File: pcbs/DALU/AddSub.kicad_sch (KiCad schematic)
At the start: 6 parts, among them U401 74HC86, U402 74HC86, U403 74HC86, U404 74HC283, U405 74HC283, U406 74HC245

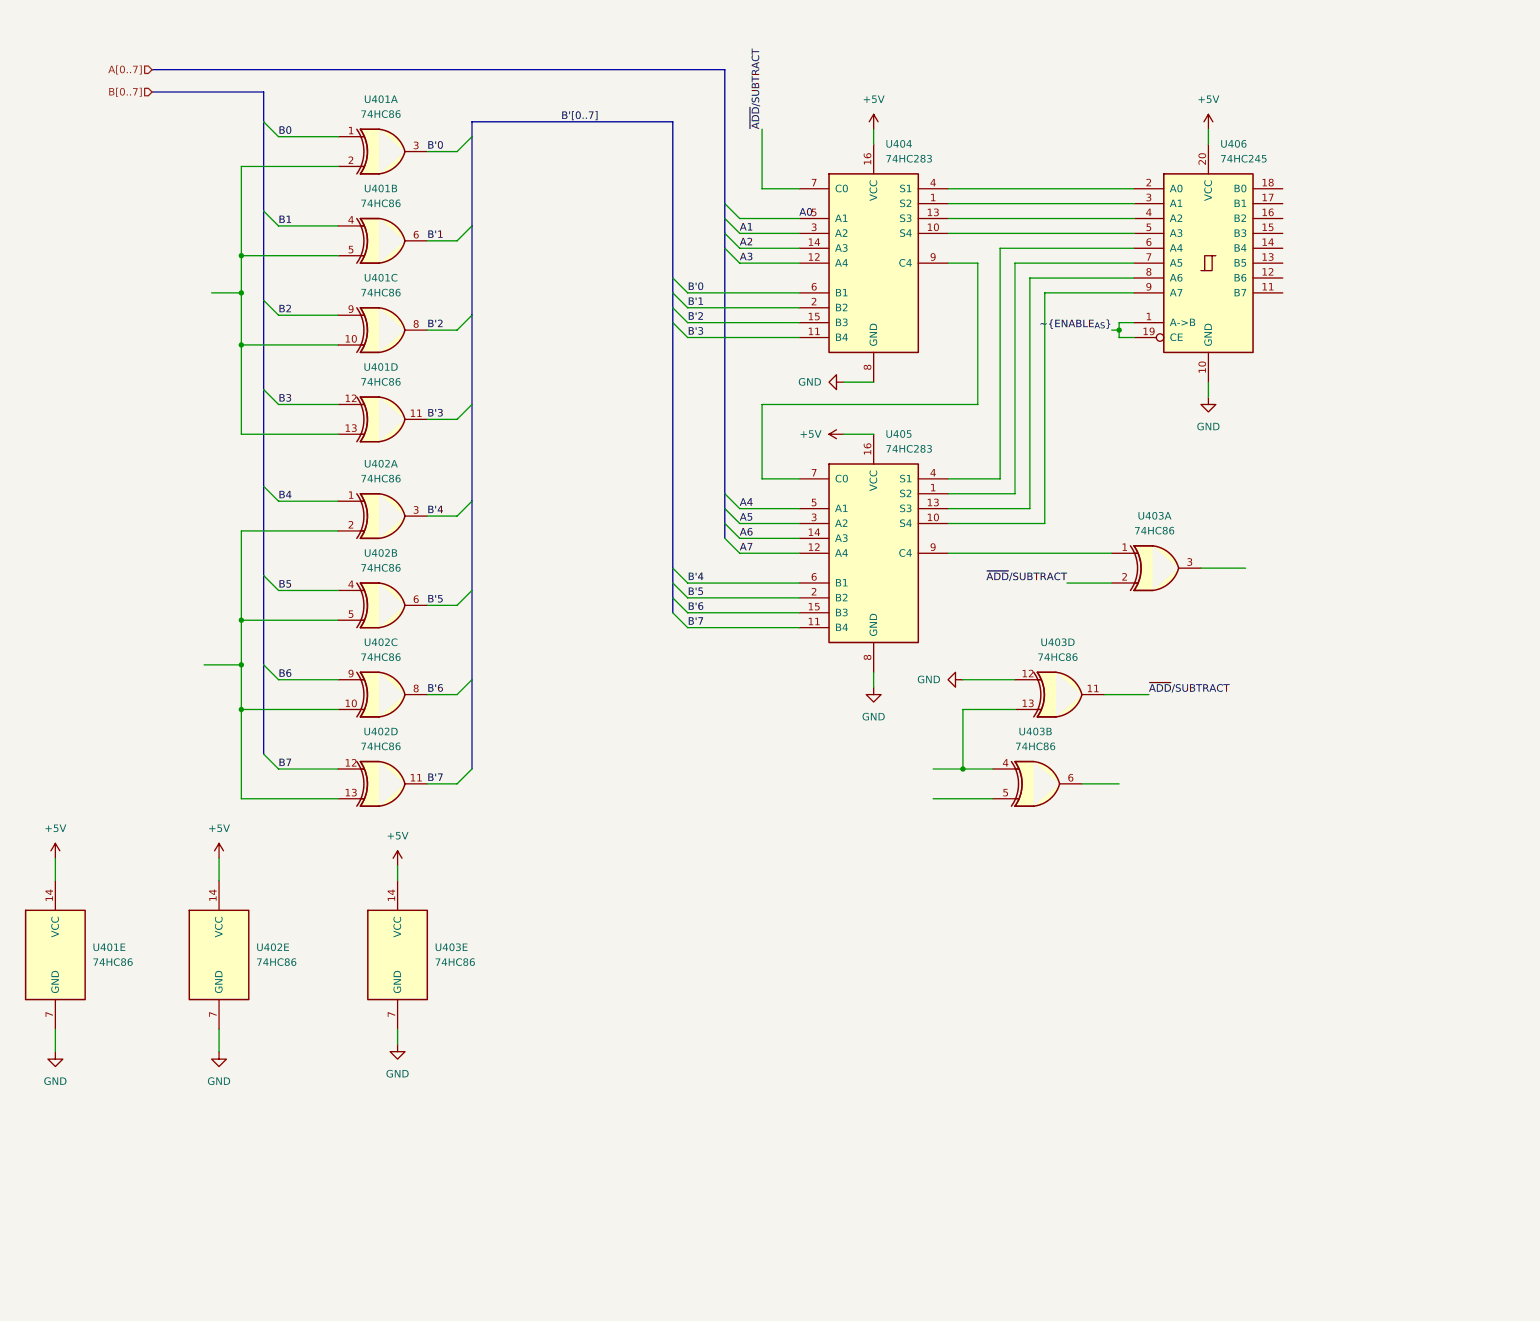
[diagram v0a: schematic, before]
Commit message: Starting to do the routing. Schematic not yet complete, though
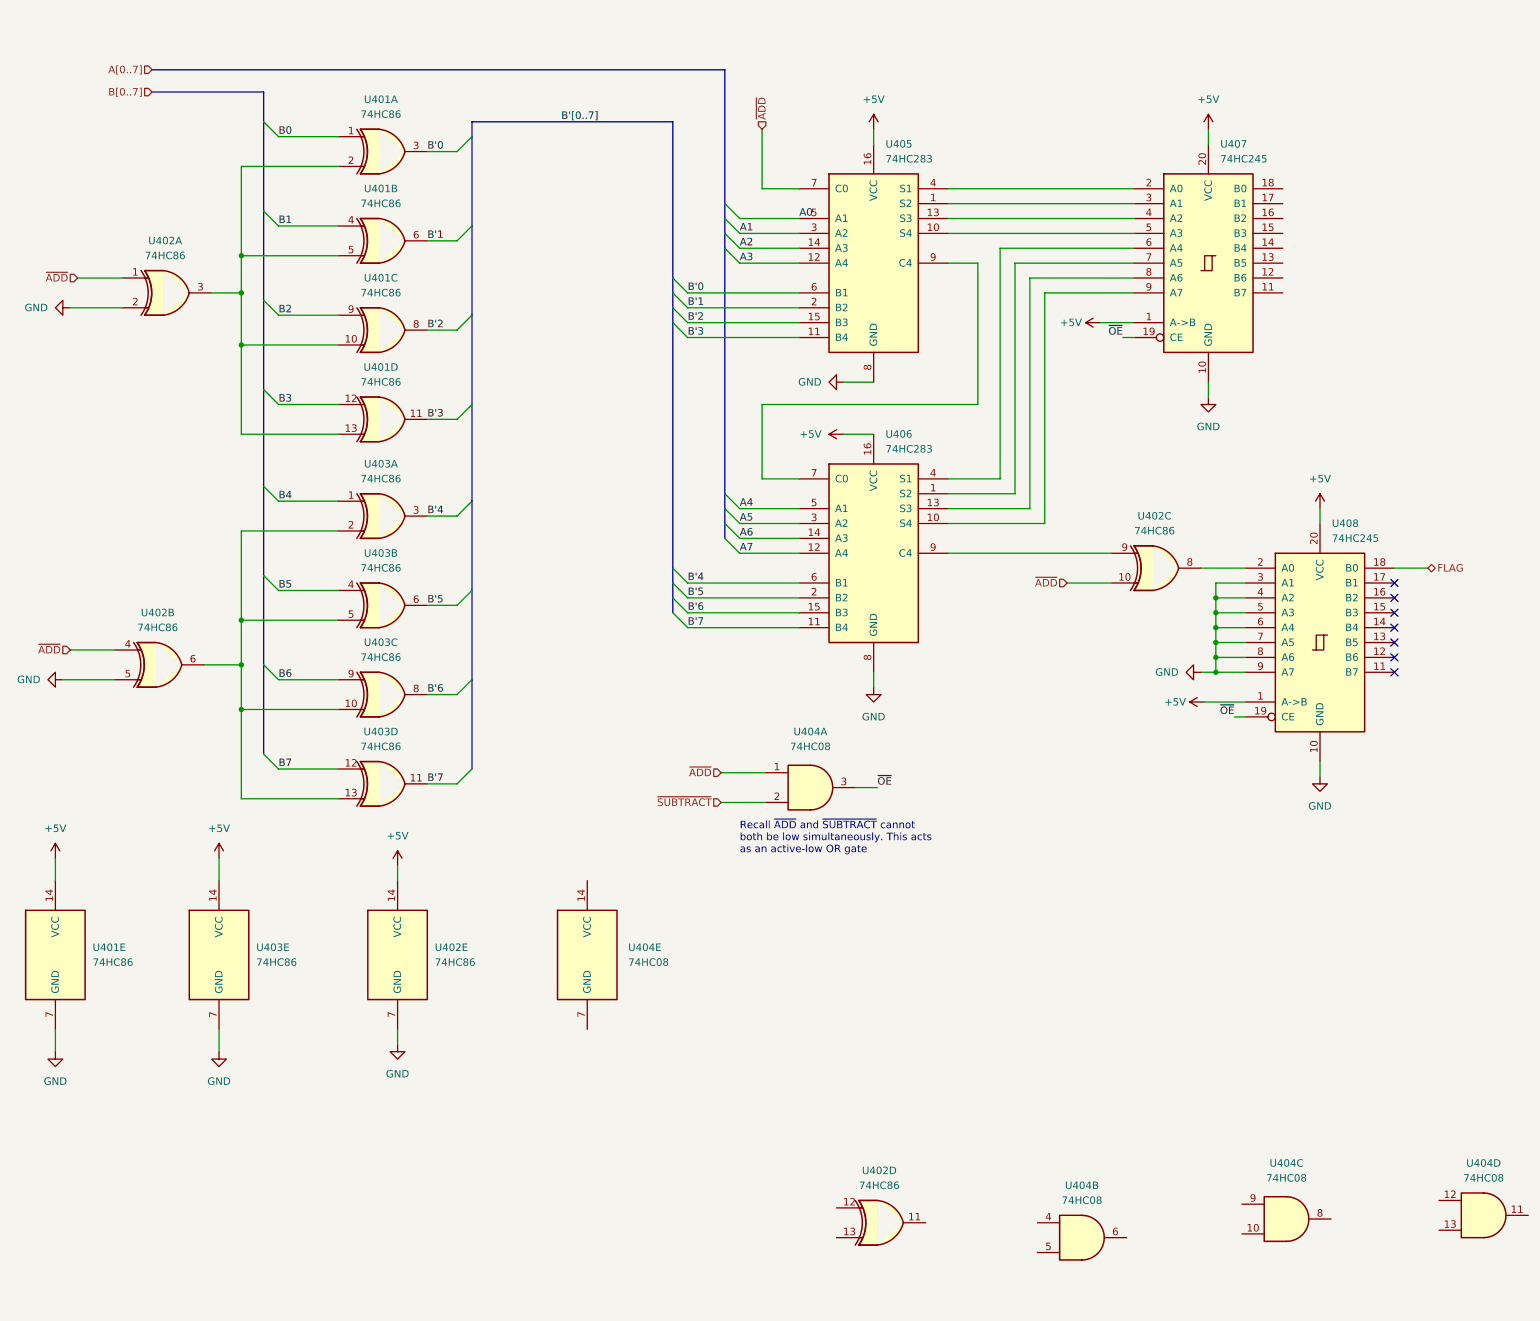
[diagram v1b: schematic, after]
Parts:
- added unit 3 of U402
- added U404: 74HC08, Package_SO:SOIC-14_3.9x8.7mm_P1.27mm, symbol 74xx:74LS08
- added U408: 74HC245, Package_SO:SOIC-20W_7.5x12.8mm_P1.27mm, symbol 74xx:74HC245
- renumbered U403 to U402, U402 to U403, U404 to U405, U405 to U406, U406 to U407
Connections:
- net +5V: now also U407.1 (A->B), U408.1 (A->B), U408.20 (VCC)
- net GND: now also U402.2, U402.5, U408.10 (GND), U408.3 (A1), U408.4 (A2), U408.5 (A3), U408.6 (A4), U408.7 (A5), U408.8 (A6), U408.9 (A7); no longer U402.12
- net at U402.13: no longer U402.4
- net at U401.10, U401.13, U401.2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: now also U402.3
- net at U402.6: now also U403.10, U403.13, U403.2, U403.5
- net at U406.9 (C4): now also U402.9; no longer U402.1
- removed net ~{ADD}/SUBTRACT: U402.11, U402.2, U405.7 (C0)
- net ~{ENABLE_{AS}} renamed ~{OE}
- net ~{OE}: now also U404.3, U408.19 (CE); no longer U407.1 (A->B)
- new net: U402.8, U408.2 (A0)
- new net FLAG: U408.18 (B0)
- new net ~{ADD}: U402.1, U402.10, U402.4, U404.1, U405.7 (C0)
- new net ~{SUBTRACT}: U404.2
- no-connect marks 0 -> 7
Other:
- note added: "Recall ~{ADD} and ~{SUBTRACT} cannot both be low simultaneously. This acts as an active-low OR gate"
- moved on the sheet: U402A, U402B, U402D

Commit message: Fiddling with the adders
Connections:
- net B'0: now also U401.8; no longer U401.3
- net B'1: now also U401.11; no longer U401.6
- net B'2: now also U401.3; no longer U401.8
- net B'3: now also U401.6; no longer U401.11
- net B'4: now also U403.8; no longer U403.3
- net B'5: now also U403.11; no longer U403.6
- net B'6: now also U403.3; no longer U403.8
- net B'7: now also U403.6; no longer U403.11
- net B0: now also U401.9; no longer U401.1
- net B1: now also U401.12; no longer U401.4
- net B2: now also U401.1; no longer U401.9
- net B3: now also U401.4; no longer U401.12
- net B4: now also U403.9; no longer U403.1
- net B5: now also U403.12; no longer U403.4
- net B6: now also U403.1; no longer U403.9
- net B7: now also U403.4; no longer U403.12
- net S_{1}: now reaches U405.1 (S2), U407.3 (A1)
- net S_{3}: now reaches U405.10 (S4), U407.5 (A3)
- net S_{2}: now reaches U405.13 (S3), U407.4 (A2)
- net S_{0}: now reaches U405.4 (S1), U407.2 (A0)
- net S_{5}: now reaches U406.1 (S2), U407.7 (A5)
- net S_{7}: now reaches U406.10 (S4), U407.9 (A7)
- net S_{6}: now reaches U406.13 (S3), U407.8 (A6)
- net S_{4}: now reaches U406.4 (S1), U407.6 (A4)
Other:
- moved on the sheet: U401A, U401B, U401C, U401D, U403A, U403B, U403C, U403D

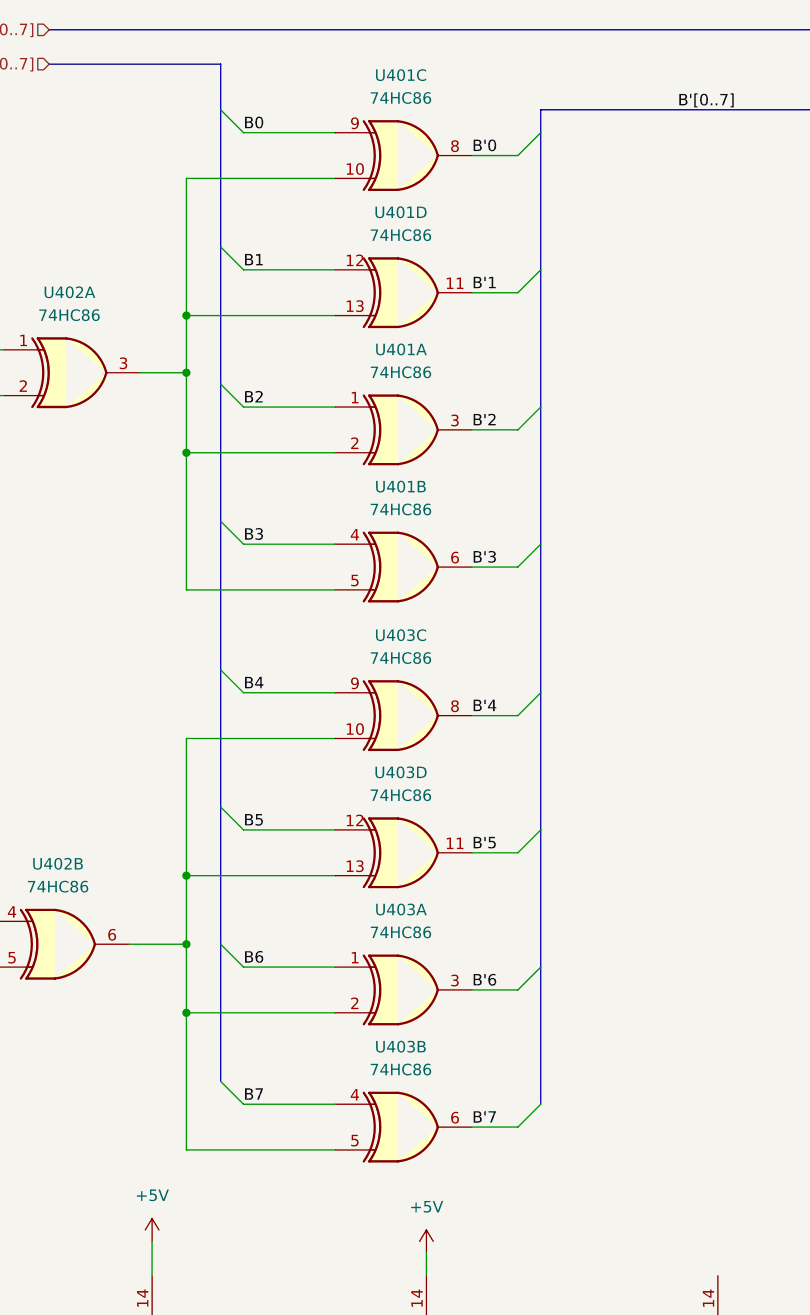
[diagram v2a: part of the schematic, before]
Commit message: Rerouting
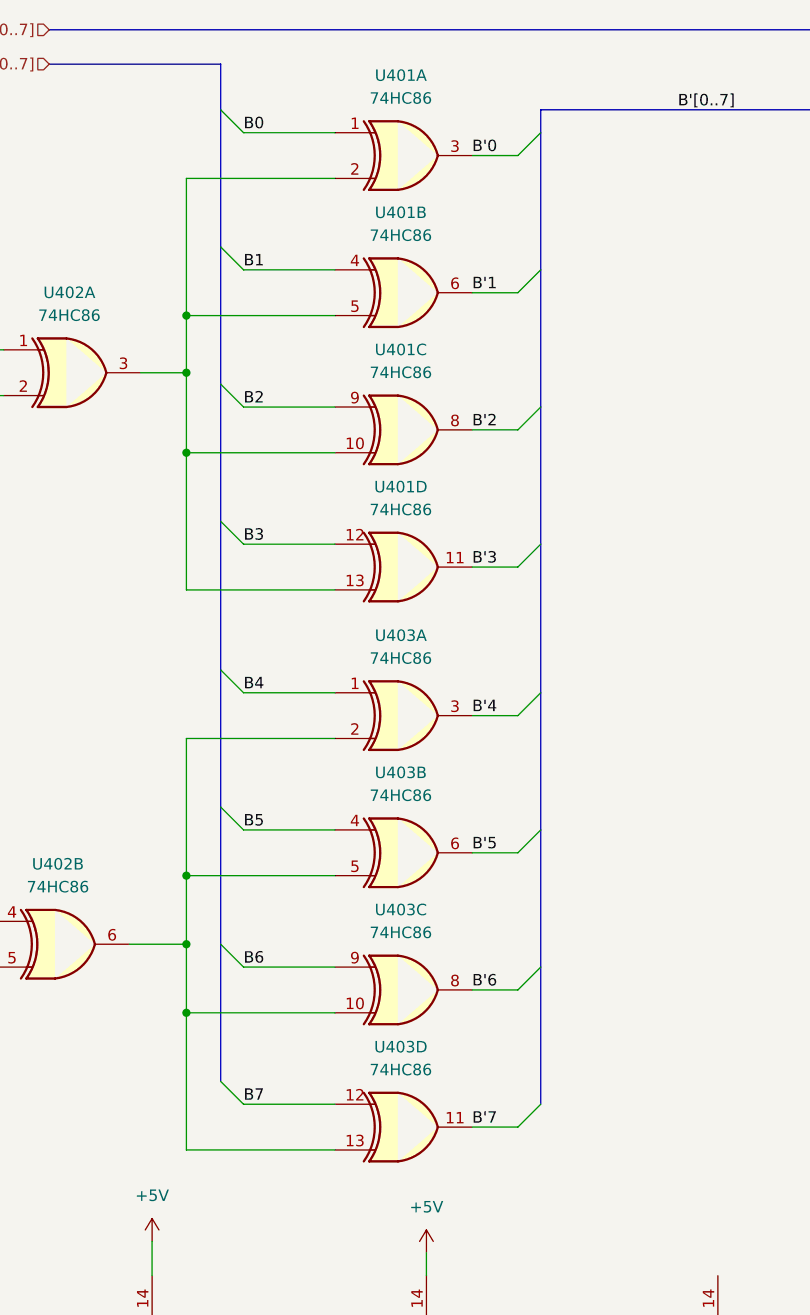
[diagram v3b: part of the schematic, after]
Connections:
- net B'0: now also U401.3; no longer U401.8
- net B'1: now also U401.6; no longer U401.11
- net B'2: now also U401.8; no longer U401.3
- net B'3: now also U401.11; no longer U401.6
- net B'4: now also U403.3; no longer U403.8
- net B'5: now also U403.6; no longer U403.11
- net B'6: now also U403.8; no longer U403.3
- net B'7: now also U403.11; no longer U403.6
- net B0: now also U401.1; no longer U401.9
- net B1: now also U401.4; no longer U401.12
- net B2: now also U401.9; no longer U401.1
- net B3: now also U401.12; no longer U401.4
- net B4: now also U403.1; no longer U403.9
- net B5: now also U403.4; no longer U403.12
- net B6: now also U403.9; no longer U403.1
- net B7: now also U403.12; no longer U403.4
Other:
- moved on the sheet: U401A, U401B, U401C, U401D, U403A, U403B, U403C, U403D

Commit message: Fixing a lot of routing
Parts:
- added C401, C402, C403, C404, C405, C406: 100n, Capacitor_SMD:C_0603_1608Metric, symbol Device:C
- renumbered U404 to U402, U402 to U404
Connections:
- net +5V: now also U402.10, U402.13, U402.14 (VCC), C401.1, C402.1, C403.1, C404.1, C405.1, C406.1
- net GND: now also U402.7 (GND), C401.2, C402.2, C403.2, C404.2, C405.2, C406.2; no longer U404.2, U404.5
- net ~{ADD}: now also U402.12, U402.9; no longer U404.1, U404.10
- net at U408.2 (A0): now also U404.6; no longer U404.8
- net at U404.9: no longer U406.9 (C4)
- net at U401.10, U401.13, U401.2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: now also U402.11; no longer U404.3
- net at U403.10, U403.13, U403.2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: now also U402.8; no longer U404.6
- new net: U404.5, U406.9 (C4)
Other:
- moved on the sheet: U402A, U402C, U402D, U402E, U404A, U404B, U404C, U408
